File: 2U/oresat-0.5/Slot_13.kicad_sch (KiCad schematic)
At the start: 2 parts

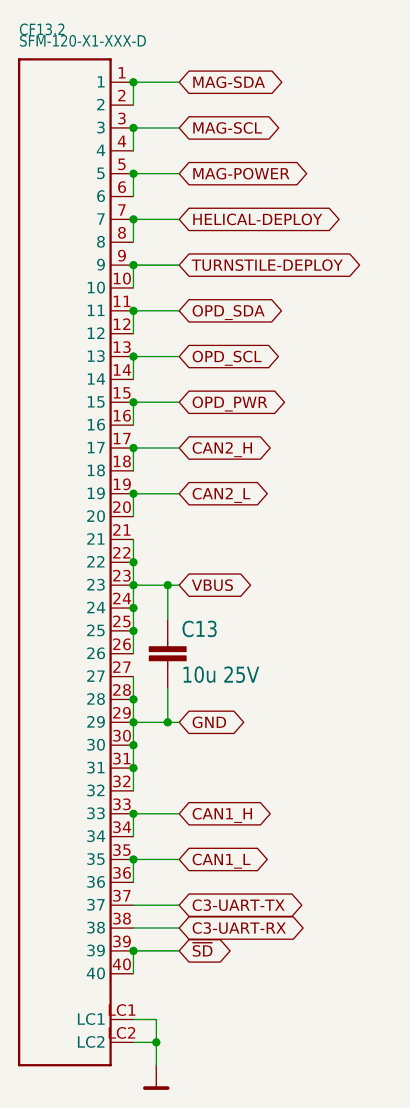
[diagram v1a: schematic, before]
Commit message: Fixed all (most) of the issues from Eagle imports
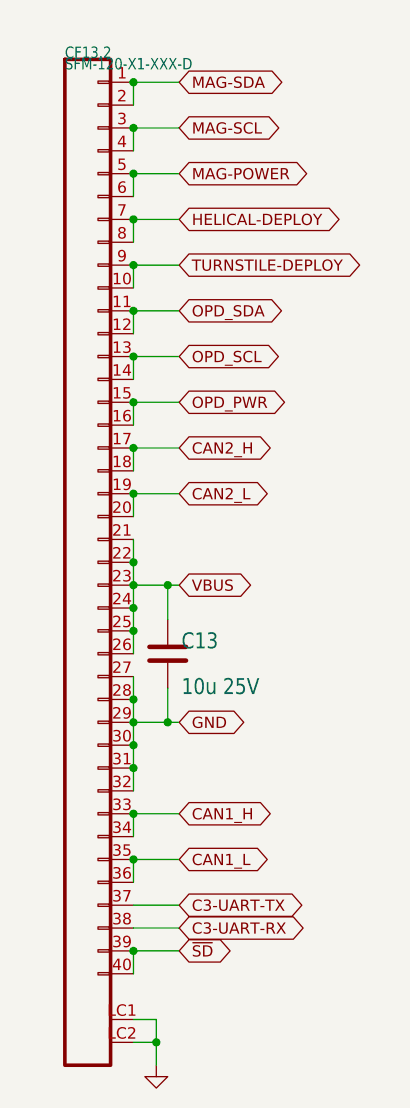
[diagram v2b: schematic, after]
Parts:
- C13: symbol oresat0-1u-backplane-eagle-import:C-EU1206-B -> Device:C
- CF13.2: symbol oresat-backplane-2u-eagle-import:SFM-120-X1-XXX-D -> oresat-connectors:J-SAMTEC-TFM-120-01-L-D-RA

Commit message: Moved entire schematic to single page
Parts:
- removed C13: 10u 25V, Capacitor_SMD:C_1206_3216Metric, symbol Device:C
- removed CF13.2: SFM-120-X1-XXX-D, oresat-connectors:J-SAMTEC-SFM-120-X1-XXX-D, symbol oresat-connectors:J-SAMTEC-TFM-120-01-L-D-RA
